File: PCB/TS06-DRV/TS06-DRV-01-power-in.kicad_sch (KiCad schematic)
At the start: 5 parts

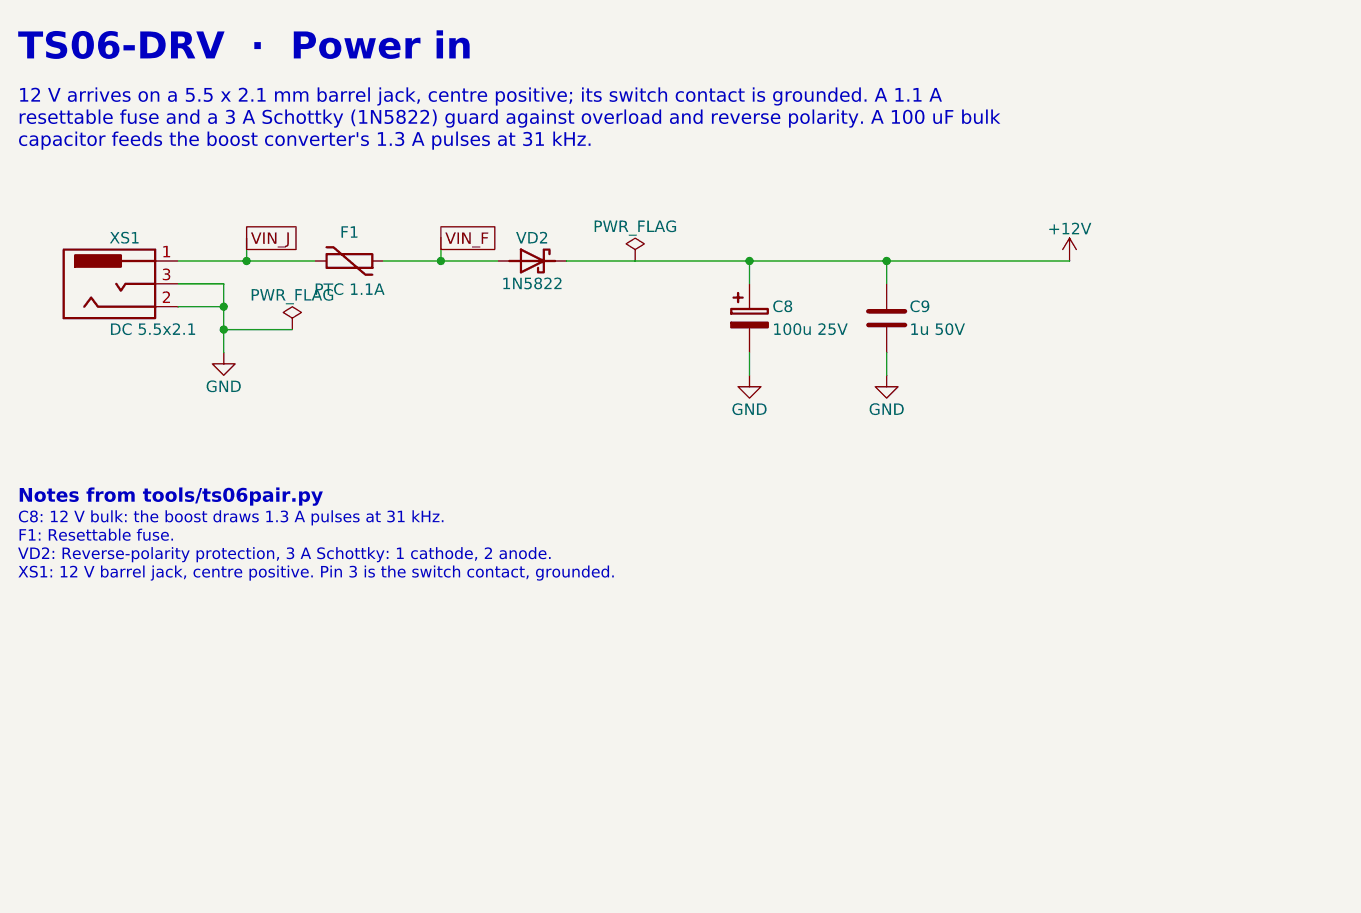
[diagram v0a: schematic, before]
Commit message: TS06-DRV rev B: routed - round 13, 0 nets sharing, 0 unrouted; board, rules and schematic written
The route of run r3 (PYTHONHASHSEED=0, the RC block of OPTIONS.md option 3),
polished (30 nets shorter), saved in tools/mkpcb_drv_routes.json, and the board
regenerated from it: check() 0 problems, 0 cathode pads under 0.5 mm, check_mate()
clean, 1164 segments, 0 vias. TS06-DRV.kicad_dru carries the 0.8 mm HV pad rule.
Schematic regenerated by tools/mksch_pair.py; BOMs unchanged by tools/bom_pair.py.

State: board written from a converged route; verify_pair not yet run.
Blocker: none.
Next: verify_pair.sh, scorecard, README row.

Co-Authored-By: Claude Opus 5.5 <noreply@anthropic.com>
Claude-Session: https://claude.ai/code/session_01WoV3gyAFgmtuk6W6Dr4bdA
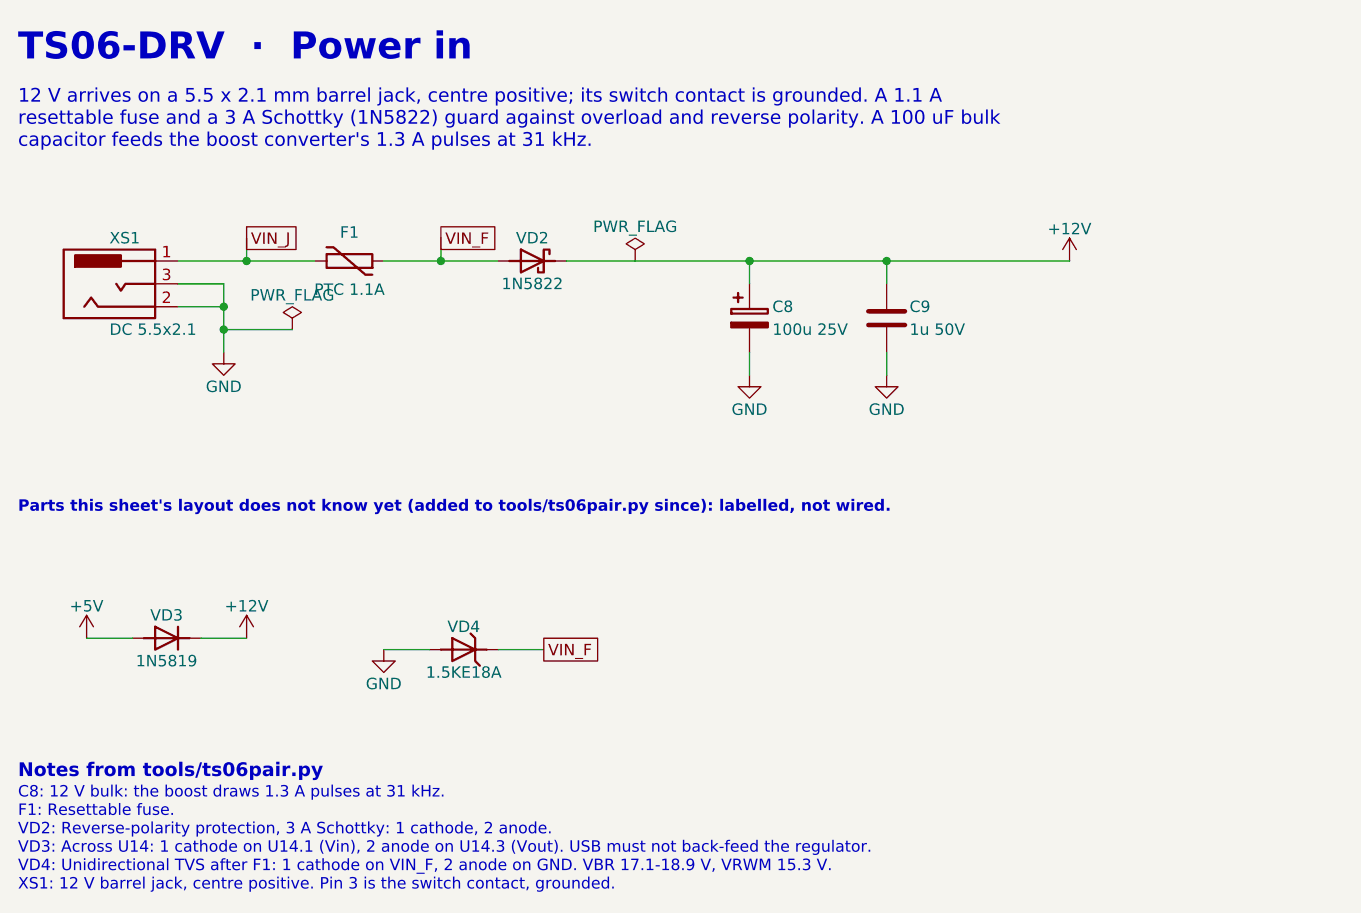
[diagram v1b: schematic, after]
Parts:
- added VD3: 1N5819, TS06:TS06_D_DO-41_P10.16mm, symbol TS06_pair:D
- added VD4: 1.5KE18A, TS06:TS06_D_DO-201AD_P15.24mm, symbol TS06_pair:D_Zener
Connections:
- net +12V: now also VD3.1 (K)
- net GND: now also VD4.2 (A)
- net VIN_F: now also VD4.1 (K)
- new net +5V: VD3.2 (A)
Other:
- note added: "C8: 12 V bulk: the boost draws 1.3 A pulses at 31 kHz. F1: Resettable fuse. VD2: Reverse-polarity protection, 3 A Schottky: 1 cathode, 2 anode. VD3: Across U14: 1 cathode on U14.1 (Vin), 2 anode on U14.3 (Vout). USB must not back-feed the regulator. VD4: Unidirectional TVS after F1: 1 cathode on VIN_F, 2 anode on GND. VBR 17.1-18.9 V, VRWM 15.3 V. XS1: 12 V barrel jack, centre positive. Pin 3 is 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"
- note added: "Parts this sheet's layout does not know yet (added to tools/ts06pair.py since): labelled, not wired."
- note removed: "C8: 12 V bulk: the boost draws 1.3 A pulses at 31 kHz. F1: Resettable fuse. VD2: Reverse-polarity protection, 3 A Schottky: 1 cathode, 2 anode. XS1: 12 V barrel jack, centre positive. Pin 3 is the switch contact, grounded."
